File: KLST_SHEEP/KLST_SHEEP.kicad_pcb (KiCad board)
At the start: 4 copper layers, 90 x 100 mm, 135 parts, among them J1 Micro_SD_Card_Card_Detect_SPI, J10 UART_00, J11 GPIO_EXT_A, J12 UART_01, J13 GPIO_EXT_B, J14 GPIO_EXT_C, J2 USB_A, J3 USB_B_Micro, J4 GPIO+AUDIO+ANALOG, J5 ARM_JTAG_SWD(STDC14), J6 HEADPHONES+MIC, J7 LINE_IN, J8 LINE_OUT, J9 I2C_00+SPI_00, Q1 AO3401A, SW1 BUTTON_BOOT_FLASH, SW2 BUTTON_RESET, SW3 ENCODER, SW4 ENCODER, SW5 ENCODER, SW6 BUTTON, U1 STM32H743VITx, U2 AMS1117-3.3, U3 WM8731SEDS, X1 KLST_SHEEP--graphics, Y1 16MHz

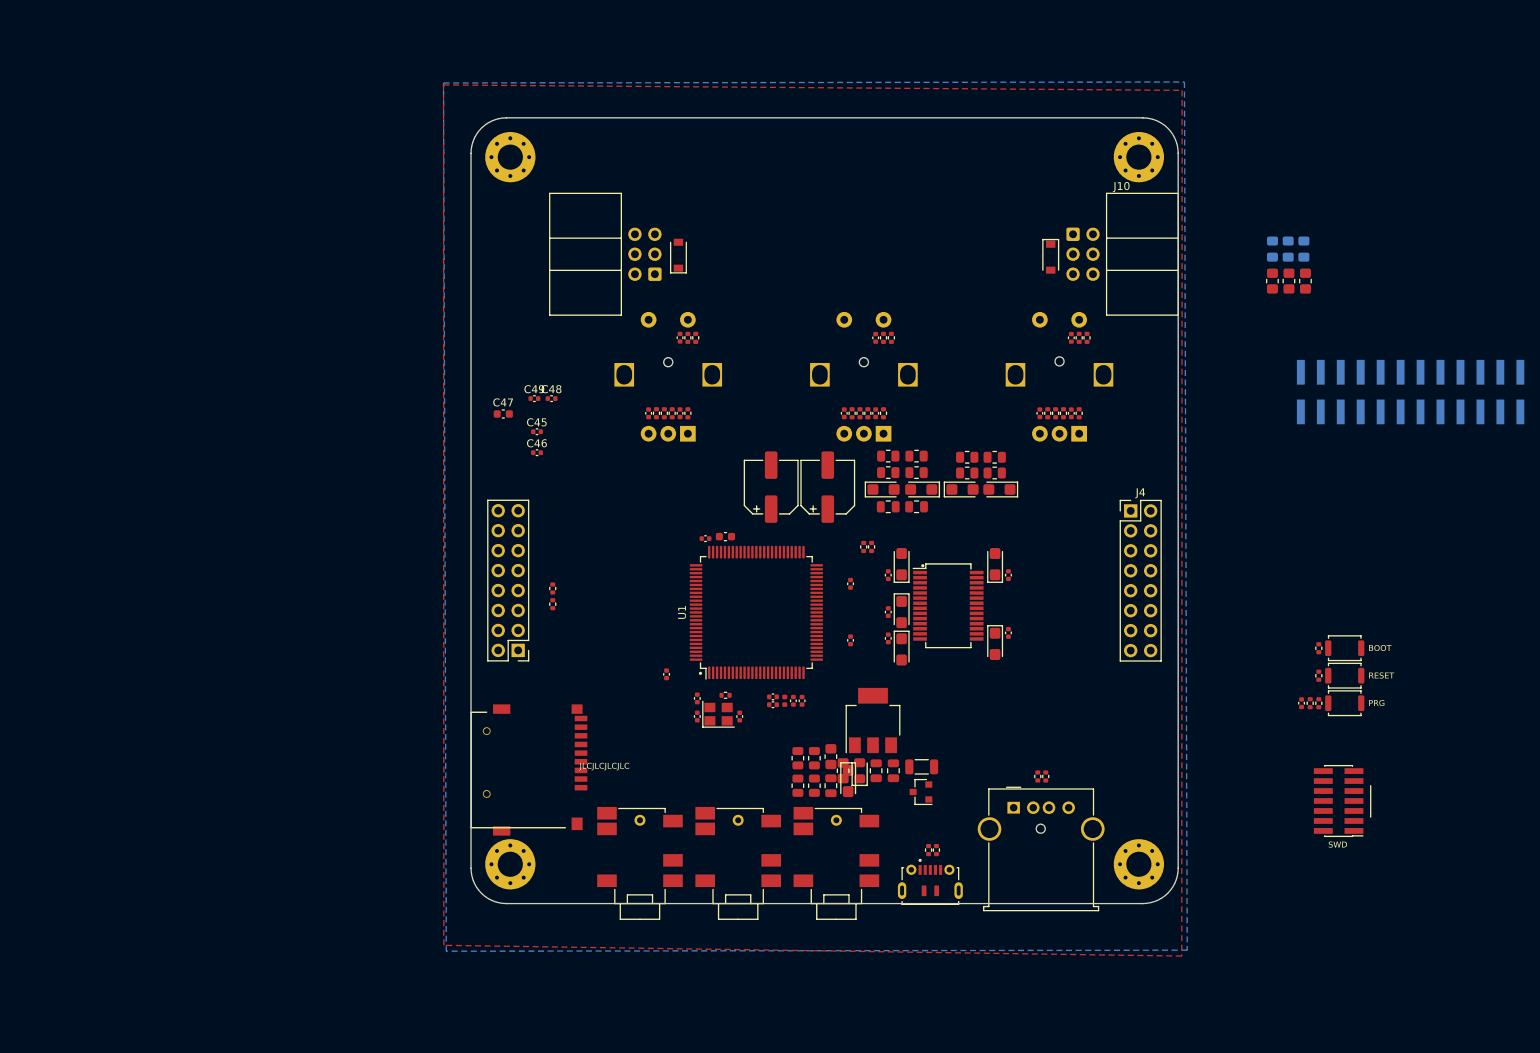
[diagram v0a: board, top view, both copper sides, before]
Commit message: reworking PCB into *handheld* version
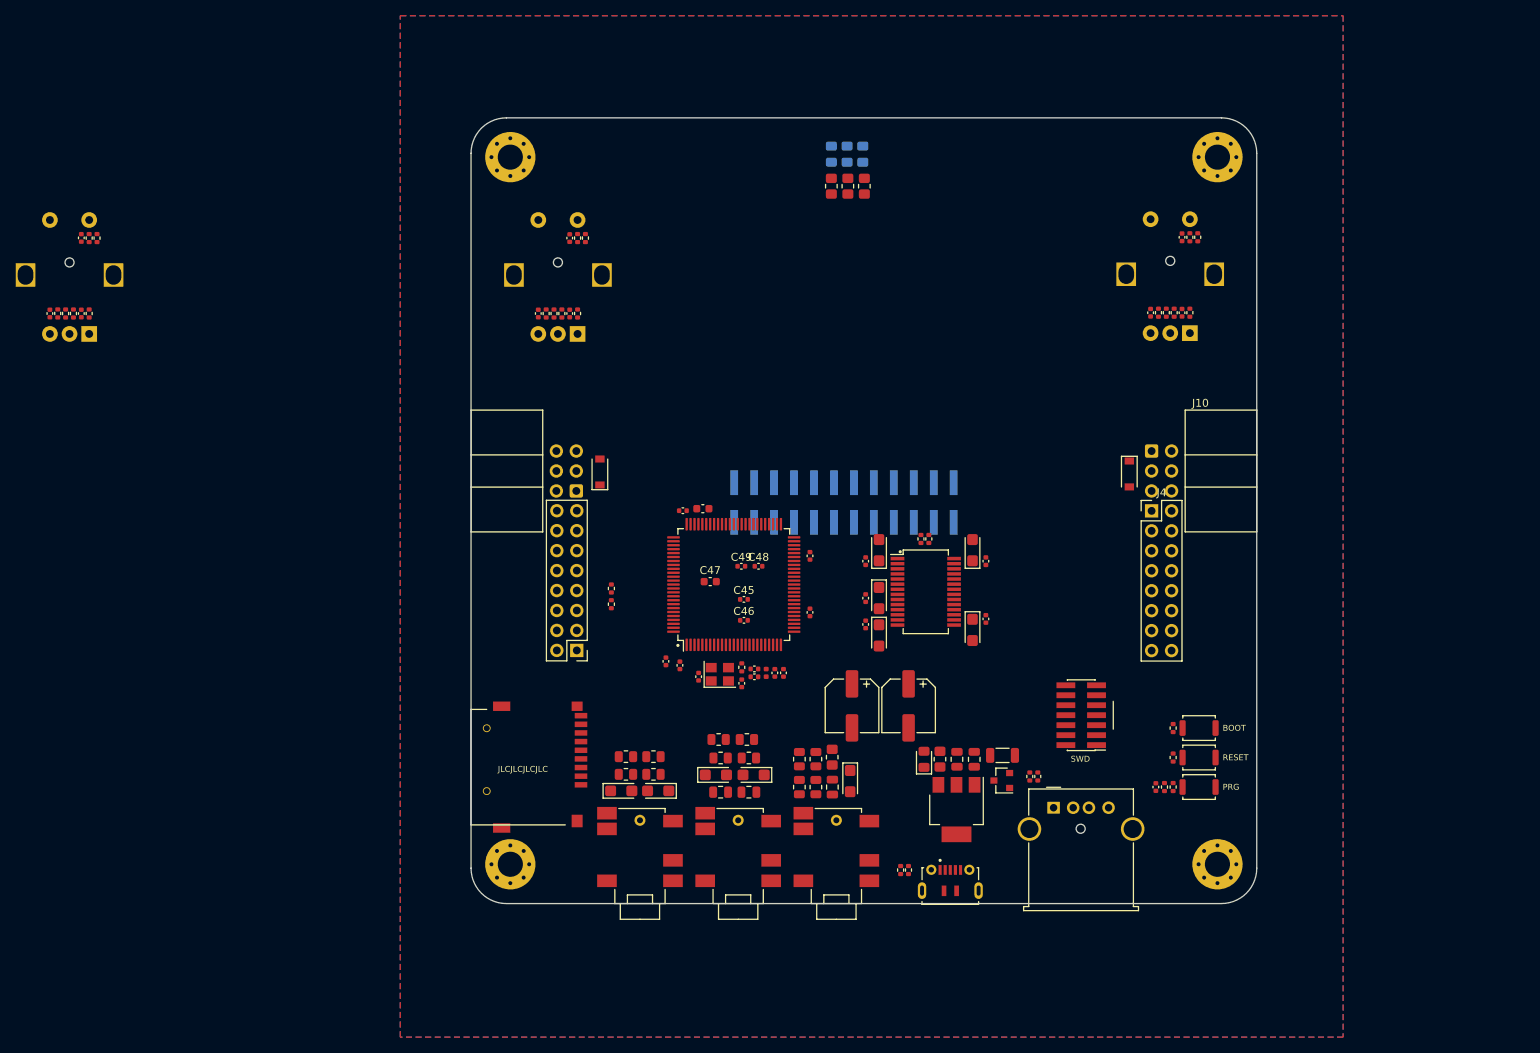
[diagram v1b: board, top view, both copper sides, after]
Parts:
- moved X1 85.9 mm to (210.2, 131.1), turned to 0 degrees
- moved C42 77.3 mm to (29.4, 68.3)
- moved R37 77.3 mm to (31.4, 68.3)
- moved R38 77.3 mm to (30.4, 68.3)
- moved R39 77.3 mm to (26.4, 77.9)
- moved SW5 77.3 mm to (30.4, 80.5)
- moved C43 77.3 mm to (29.4, 77.9)
- moved C44 77.3 mm to (25.4, 77.9)
- moved R40 77.3 mm to (30.4, 77.9)
- moved R41 77.3 mm to (28.4, 77.9)
- moved R42 77.3 mm to (27.4, 77.9)
- moved J13 73.5 mm to (126.5, 102.0)
- moved J14 73.5 mm to (136.6, 102.0)
- moved J11 73.5 mm to (116.3, 102.0)
- moved C27 57.9 mm to (98.1, 138.7)
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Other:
- board size 90 x 100 mm -> 151.7 x 100 mm
- board text added: "IDEA: - upper part is separable - it hosts 2(!) encoder + 2–4 push buttons - it makes spaces for an LCD display ( optional ) - a bit like a switch or PSP - KLST is held upside down ( cables on top, controllers at the bottom )"

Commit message: minor changes
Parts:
- removed C49: 100nF, Capacitor_SMD:C_0402_1005Metric
- moved C48 15.3 mm to (102.7, 118.4), turned to 180 degrees
- moved C47 13.9 mm to (122.6, 107.6)
- moved C45 8.14 mm to (116.0, 122.1), turned to 270 degrees
- moved C13 7.41 mm to (111.2, 121.7), turned to 180 degrees
- moved R43 5.91 mm to (102.3, 115.2), turned to 0 degrees
- moved R44 5.48 mm to (102.3, 114.2), turned to 0 degrees
- moved C46 5.30 mm to (115.0, 122.1), turned to 270 degrees
- moved C7 3.82 mm to (118.3, 122.1), turned to 270 degrees
- moved C11 3.47 mm to (109.0, 122.1)
- moved C8 2.46 mm to (117.3, 122.1), turned to 270 degrees
- moved C14 2.34 mm to (122.1, 106.4), turned to 0 degrees
- moved C12 1.96 mm to (122.1, 117.9), turned to 0 degrees
- moved C1 1.66 mm to (109.6, 124.4), turned to 90 degrees
- moved Y1 1.64 mm to (112.3, 124.0)
- moved C2 1.64 mm to (115.0, 124.4), turned to 270 degrees
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
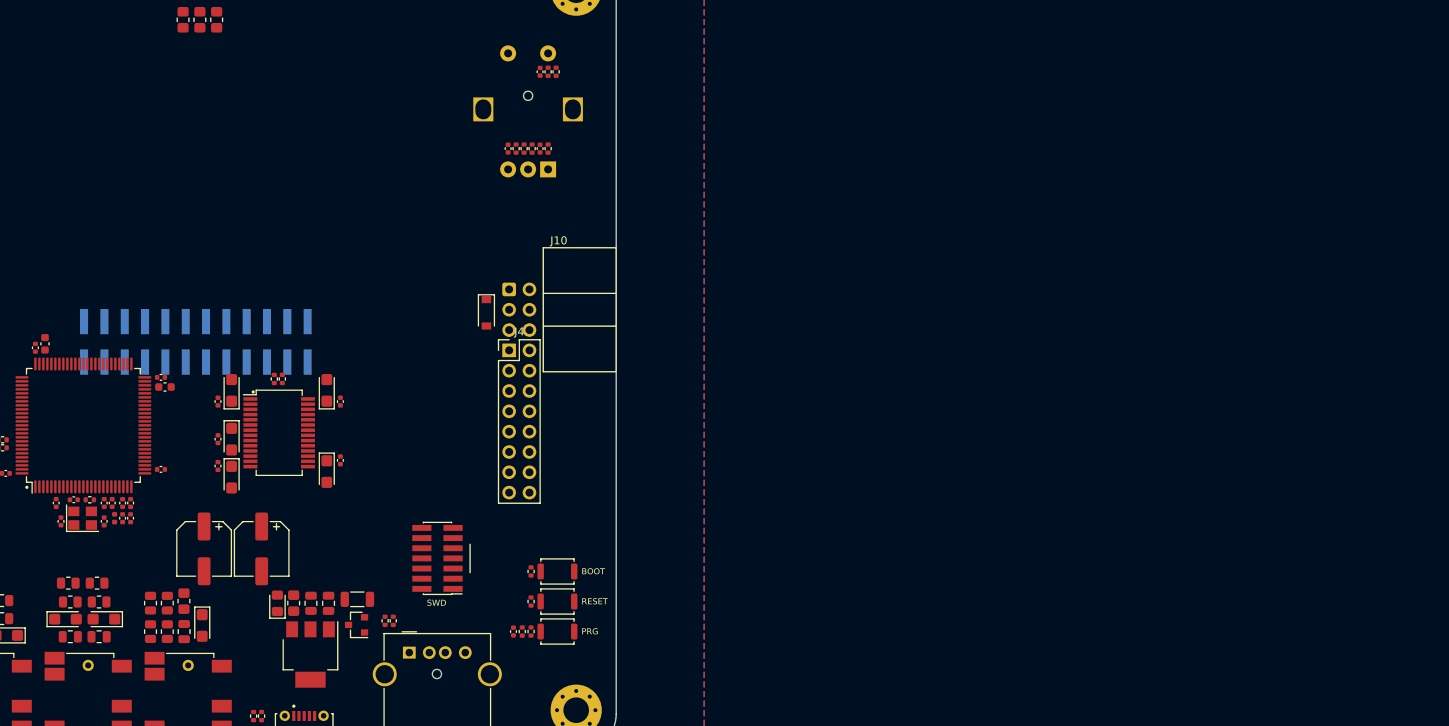
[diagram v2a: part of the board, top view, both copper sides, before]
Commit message: added NHD display
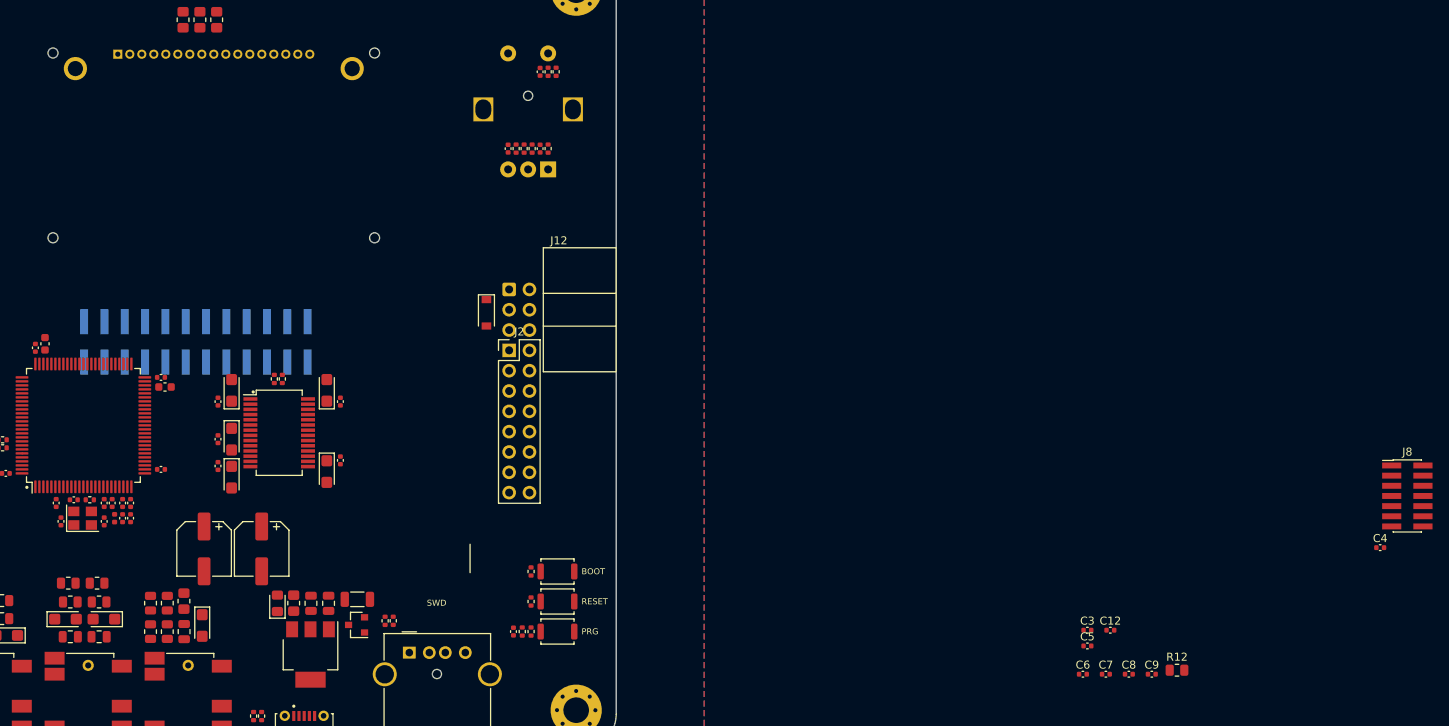
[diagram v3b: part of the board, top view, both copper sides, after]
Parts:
- removed the J5 at (156.7, 129.0)
- added C12: 1uF, Capacitor_SMD:C_0402_1005Metric, F.Cu at (240.8, 138.0)
- added C3: 1uF, Capacitor_SMD:C_0402_1005Metric, F.Cu at (237.9, 138.0)
- added C4: 100nF, Capacitor_SMD:C_0402_1005Metric, F.Cu at (274.5, 127.7)
- added C5: 1uF, Capacitor_SMD:C_0402_1005Metric, F.Cu at (237.9, 140.0)
- added C6: 100nF, Capacitor_SMD:C_0402_1005Metric, F.Cu at (237.3, 143.5)
- added C7: 100nF, Capacitor_SMD:C_0402_1005Metric, F.Cu at (240.2, 143.5)
- added C8: 100nF, Capacitor_SMD:C_0402_1005Metric, F.Cu at (243.1, 143.5)
- added C9: 100nF, Capacitor_SMD:C_0402_1005Metric, F.Cu at (245.9, 143.5)
- added DS1: NHD-C12832A1Z-FSW-FBW-3V3, KLST_TINY:Newhaven_Display-NHD-C12832A1Z-FSW-FBW-3V3, B.Cu at (128.7, 77.4)
- added J8: ARM_JTAG_SWD(STDC14), Connector_PinHeader_1.27mm:PinHeader_2x07_P1.27mm_Vertical_SMD, F.Cu at (277.9, 121.2)
- added R12: R_Small, Resistor_SMD:R_0805_2012Metric, F.Cu at (249.1, 143.0)
- renumbered C4 to C10, C5 to C11, C7 to C13, C8 to C14, C45 to C15, C46 to C16, C47 to C17, C9 to C18, C10 to C19, C11 to C20, C12 to C21, C13 to C22, C14 to C23, C15 to C24, C48 to C25, C6 to C26, C16 to C27, C17 to C28, C18 to C29, C19 to C30, C20 to C31, C21 to C32, C22 to C33, C23 to C34, C24 to C35, C25 to C36, C26 to C37, C27 to C38, C28 to C39, C29 to C40, C30 to C41, C31 to C42, C32 to C43, C33 to C44, C34 to C45, C35 to C46, C36 to C47, C37 to C48, C38 to C49, C39 to C50, C40 to C51, C41 to C52, C42 to C53, C43 to C54, C44 to C55, C3 to C56, J7 to J10, J8 to J11, J10 to J12, J9 to J13, J12 to J14, J4 to J2, J2 to J3, J11 to J4, J3 to J5, J13 to J6, J14 to J7, J6 to J9, R8 to R10, R9 to R11, R10 to R13, R11 to R14, R12 to R15, R13 to R16, R14 to R17, R15 to R18, R16 to R19, R47 to R2, R17 to R20, R18 to R21, R19 to R22, R20 to R23, R21 to R24, R22 to R25, R23 to R26, R24 to R27, R25 to R28, R26 to R29, R2 to R3, R27 to R30, R28 to R31, R29 to R32, R30 to R33, R31 to R34, R32 to R35, R33 to R36, R34 to R37, R35 to R38, R36 to R39, R48 to R4, R37 to R40, R38 to R41, R39 to R42, R40 to R43, R41 to R44, R42 to R45, R44 to R46, R43 to R47, R45 to R48, R46 to R49, R4 to R5, R5 to R6, R6 to R7, R7 to R8, R3 to R9
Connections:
- U1 pad 77: /SWD_SWI -> /GPIO_EXT_A_07
- U1 pad 78: /GPIO_EXT_A_07 -> /GPIO_EXT_A_06
- U1 pad 79: /GPIO_EXT_A_06 -> /GPIO_EXT_A_05
- U1 pad 80: /GPIO_EXT_A_05 -> /GPIO_EXT_A_04
- U1 pad 81: /GPIO_EXT_A_04 -> /GPIO_EXT_A_03
- U1 pad 82: /GPIO_EXT_A_03 -> /GPIO_EXT_A_02
- U1 pad 83: /GPIO_EXT_A_02 -> /GPIO_EXT_A_01
- U1 pad 84: /GPIO_EXT_A_01 -> /GPIO_EXT_A_00
- U1 pad 85: /GPIO_EXT_A_00 -> (no net)
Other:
- board text added: "TODO: - update GPIO++ - fit display"

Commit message: added screen, added icon
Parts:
- removed C53, C54, C55: 100nF, Capacitor_SMD:C_0402_1005Metric
- removed R40, R42, R43, R44, R45: 10K, Resistor_SMD:R_0402_1005Metric
- removed R41: 1K, Resistor_SMD:R_0402_1005Metric
- removed SW5: ENCODER, Rotary_Encoder:RotaryEncoder_Alps_EC12E-Switch_Vertical_H20mm
- added J15: GMT028-05_V1.1, Connector_PinSocket_2.54mm:PinSocket_1x07_P2.54mm_Vertical, B.Cu at (122.5, 60.0)
- added X2: KLST_SHEEP--icon, KLST_TINY:KLST_SHEEP--icon, B.Cu at (167.7, 118.7)
- R12: value R_Small -> 30R
- moved C4 168.4 mm to (118.0, 65.5), turned to 270 degrees
- moved R12 153.8 mm to (115.8, 66.3), turned to 270 degrees
- moved J8 149.8 mm to (130.5, 94.6), turned to 90 degrees
- moved C9 144.8 mm to (124.0, 65.5), turned to 270 degrees
- moved C8 143.6 mm to (122.5, 65.5), turned to 270 degrees
- moved C7 142.5 mm to (121.0, 65.5), turned to 270 degrees
- moved C6 141.3 mm to (119.5, 65.5), turned to 270 degrees
- moved C5 134.8 mm to (125.5, 65.5), turned to 90 degrees
- moved C3 131.2 mm to (128.5, 65.5), turned to 270 degrees
- moved C12 131.1 mm to (131.5, 65.5), turned to 270 degrees
- moved X1 119.2 mm to (93.8, 105.5), turned to 180 degrees
- moved J13 96.9 mm to (152.2, 44.6), turned to 90 degrees
- moved J14 87.4 mm to (172.0, 136.6), turned to 270 degrees
- moved J12 83.4 mm to (93.1, 136.6), turned to 270 degrees
- moved D6 82.4 mm to (169.5, 134.1), turned to 180 degrees
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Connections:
- J8 pad 13: /SERIAL_DEBUG_TX -> /SERIAL_DEBUG_RX
- J8 pad 14: /SERIAL_DEBUG_RX -> /SERIAL_DEBUG_TX
- U1 pad 90: /ENCODER_02_A -> (no net)
- U1 pad 91: /ENCODER_02_B -> (no net)
- U1 pad 95: /ENCODER_02_BUTTON -> (no net)
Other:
- board size 151.7 x 100 mm -> 100 x 100 mm
- board text added: "TODO: - update GPIO++ - fit display - space out programmer boot/rst/buttons"
- board text removed: "TODO: - update GPIO++ - fit display"

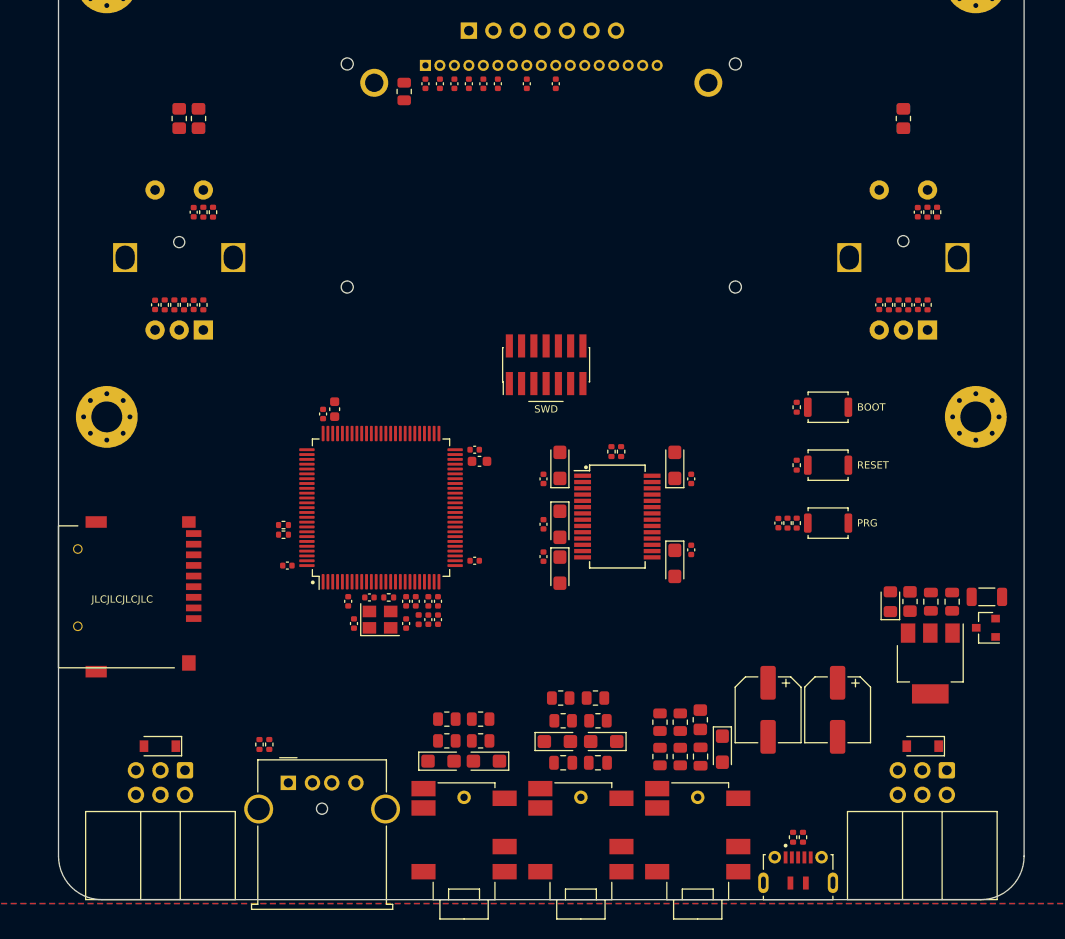
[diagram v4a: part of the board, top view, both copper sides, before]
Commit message: updated capabilites, updated GPIOs
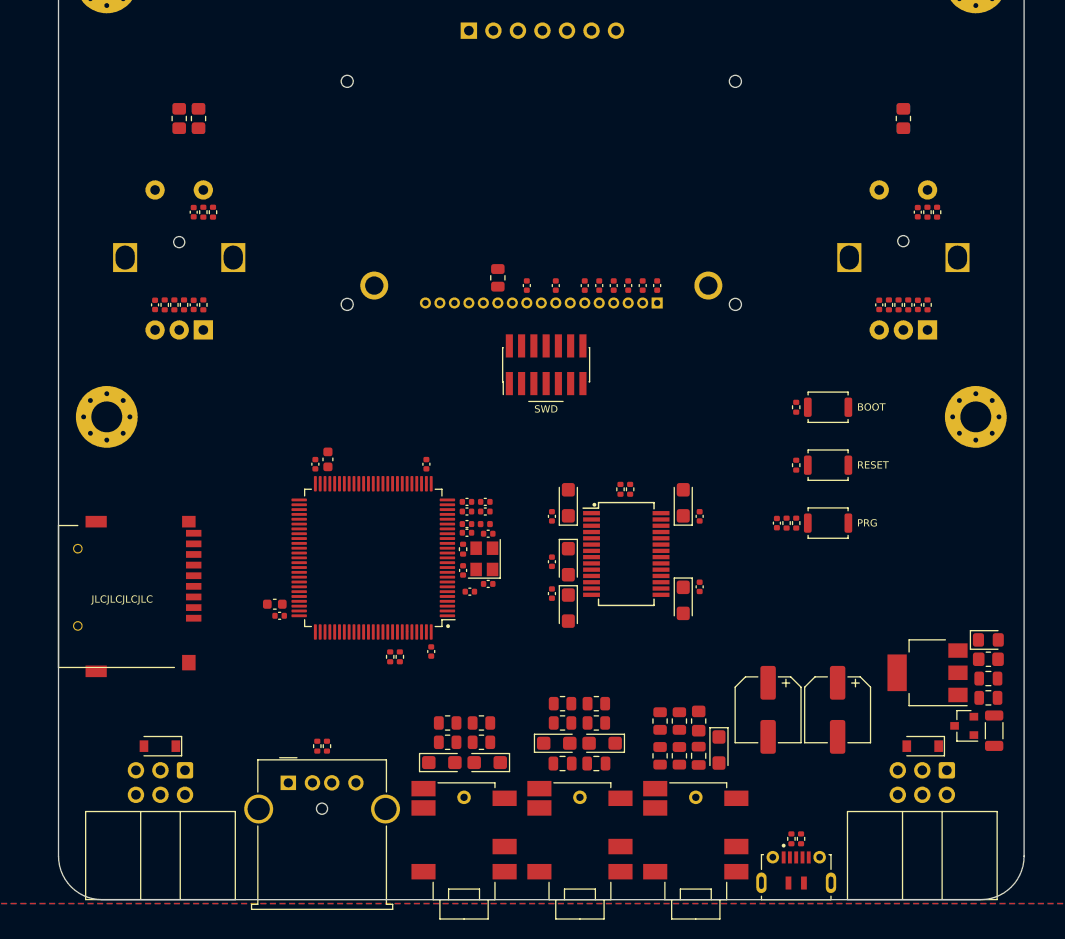
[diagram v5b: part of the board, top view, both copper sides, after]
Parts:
- DS1: footprint KLST_TINY:Newhaven_Display-NHD-C12832A1Z-FSW-FBW-3V3 -> KLST_SHEEP:Newhaven_Display-NHD-C12832A1Z-FSW-FBW-3V3
- X2: footprint KLST_TINY:KLST_SHEEP--icon -> KLST_SHEEP:KLST_SHEEP--icon
- moved C4 31.8 mm to (142.0, 86.4), turned to 90 degrees
- moved C6 29.6 mm to (140.5, 86.4), turned to 90 degrees
- moved C7 27.6 mm to (139.0, 86.4), turned to 90 degrees
- moved C8 25.7 mm to (137.5, 86.4), turned to 90 degrees
- moved C9 24.1 mm to (136.0, 86.4), turned to 90 degrees
- moved C5 22.8 mm to (134.5, 86.4), turned to 270 degrees
- moved R12 21.6 mm to (125.5, 85.6)
- moved C24 21.4 mm to (102.9, 120.6), turned to 180 degrees
- moved C26 21.1 mm to (102.4, 119.4), turned to 180 degrees
- moved C12 21.1 mm to (128.5, 86.4), turned to 90 degrees
- moved C3 21.1 mm to (131.5, 86.4), turned to 90 degrees
- moved R46 17.6 mm to (114.3, 124.8), turned to 90 degrees
- moved R47 17.5 mm to (115.3, 124.8), turned to 90 degrees
- moved C25 17.4 mm to (118.6, 124.3), turned to 270 degrees
- moved C23 16.6 mm to (106.6, 104.9), turned to 90 degrees
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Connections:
- J4 pad 3: /GPIO_EXT_A_02 -> (no net)
- J4 pad 4: /GPIO_EXT_A_03 -> (no net)
- J4 pad 5: /GPIO_EXT_A_04 -> (no net)
- J4 pad 6: /GPIO_EXT_A_05 -> (no net)
- J4 pad 7: /GPIO_EXT_A_06 -> (no net)
- J4 pad 8: /GPIO_EXT_A_07 -> (no net)
- U1 pad 79: /GPIO_EXT_A_05 -> (no net)
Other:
- net class Default: trace_width 0.25 -> 0.2; via_dia 0.8 -> 0.4; via_drill 0.4 -> 0.2
- rule via_min_drill: 0.3 -> 0.2

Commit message: cleaned up
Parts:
- moved R5 6.14 mm to (90.5, 63.3)
- moved R7 6.14 mm to (92.5, 63.3)
- moved D1 4.21 mm to (90.5, 65.4)
- moved D3 4.21 mm to (92.5, 65.4)
- moved J4 3.20 mm to (89.3, 43.3)
- moved J6 2.00 mm to (100.7, 43.3)
- moved C16 0.10 mm to (122.3, 112.1)
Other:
- outline, holes or cut-outs redrawn
